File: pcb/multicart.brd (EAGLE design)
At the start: 55.5 x 85.1 mm, 13 parts, among them IC1 74HCT373N, IC2 M27C4001B, Q1 BS170

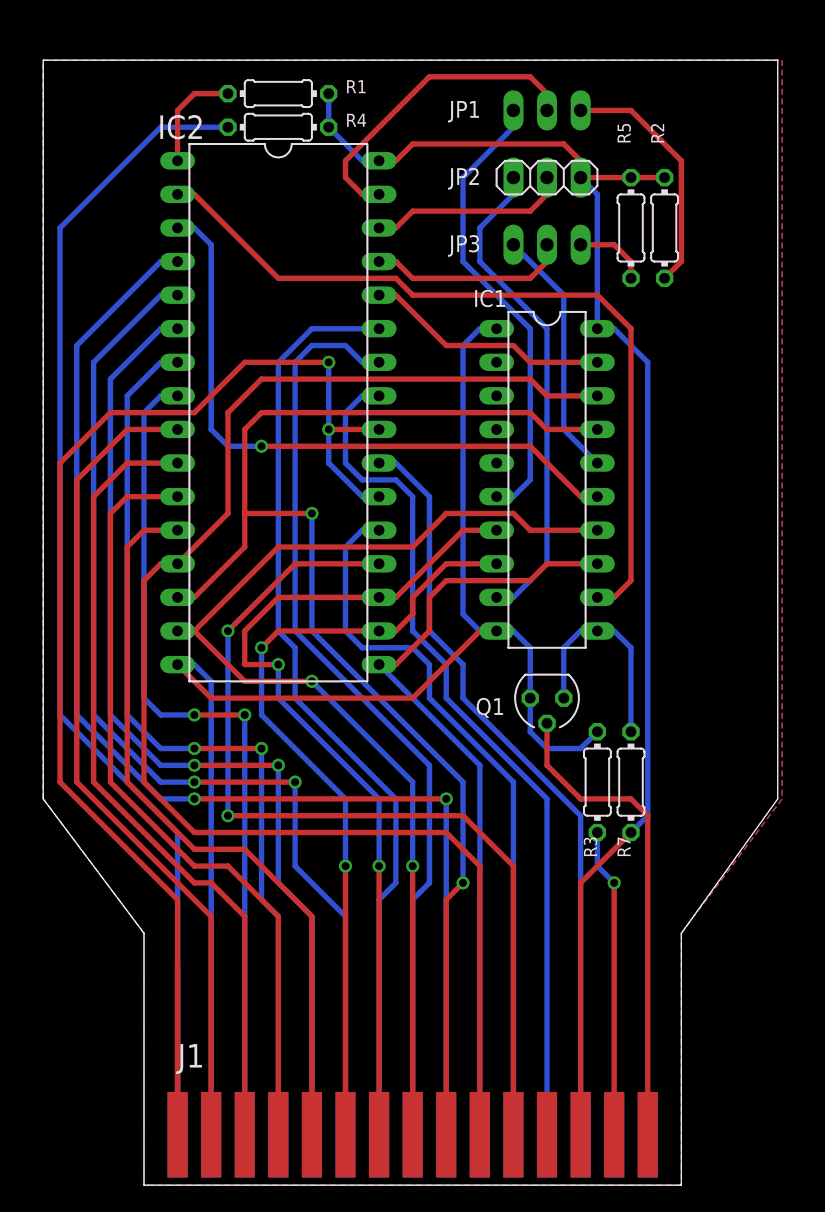
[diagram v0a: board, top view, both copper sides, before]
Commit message: Swapped cart bank mapping & reorganized the PCB.
Fixes #1
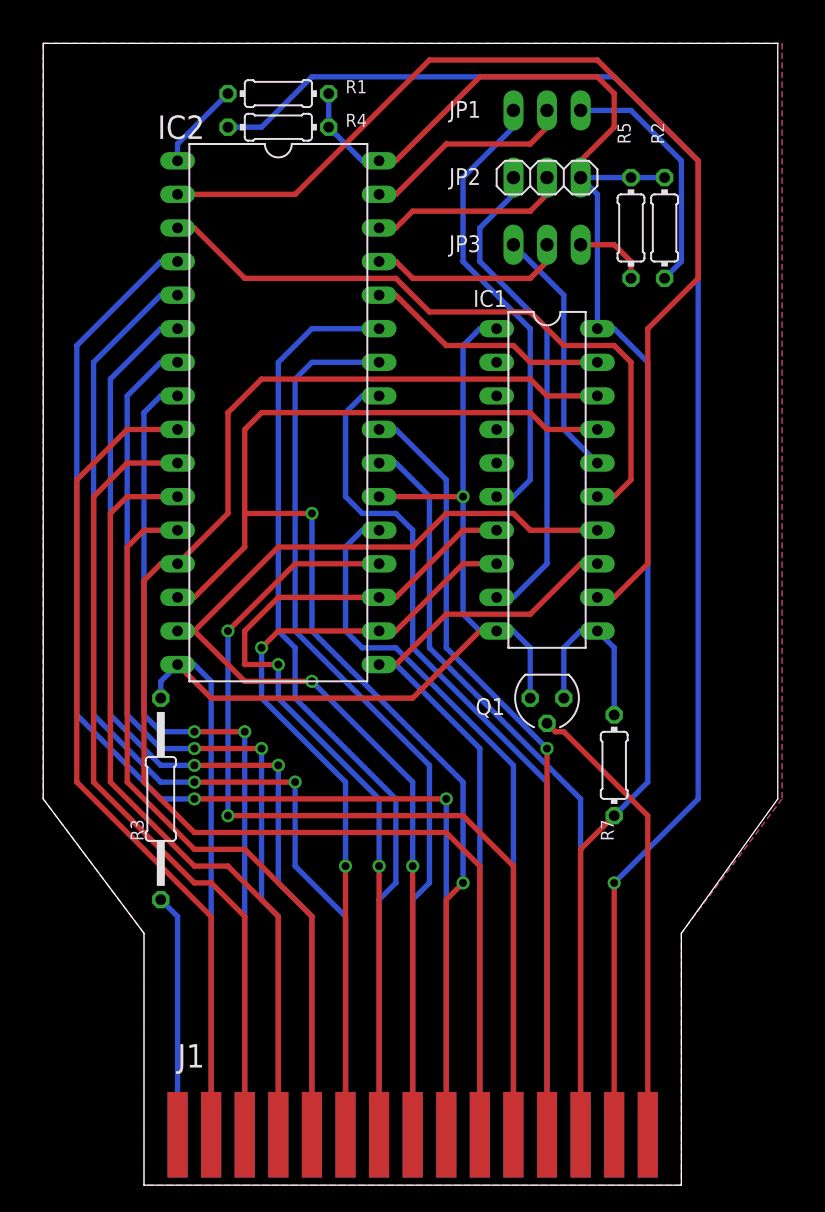
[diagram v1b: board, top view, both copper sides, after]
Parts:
- R3: device resistor:0204/7 -> resistor:0207/15
- moved R3 33.0 mm to (15.2, 26.7)
- moved R7 1.80 mm to (49.5, 29.2)
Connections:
- net GND: now also IC2.22
- net N$13: now also J1.14; no longer J1.A
- net N$14: now also J1.A; no longer J1.14
- net N$17: now also J1.12; no longer IC2.22, J1.1
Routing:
- net N$17: track 107.0 -> 59.3 mm, vias 2 -> 1
- net N$13: track 88.1 -> 116.1 mm, vias 0 -> 1
- net N$4: track 60.6 -> 83.7 mm
- net VCC: track 108.7 -> 119.4 mm
- net N$10: track 24.0 -> 16.1 mm
- net N$14: track 23.4 -> 18.3 mm, vias 1 -> 0
- net N$7: track 16.3 -> 13.8 mm
- net N$3: track 48.4 -> 50.5 mm, vias 1 -> 0
- net N$8: track 36.5 -> 34.6 mm
- net A9: track 70.6 -> 68.8 mm
- net N$9: track 8.15 -> 6.66 mm
- net GND: track 106.6 -> 107.4 mm, vias 0 -> 1
- net D3: track 59.9 -> 59.1 mm
- net D7: track 55.0 -> 54.3 mm
- net D4: track 60.6 -> 59.9 mm
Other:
- board size 55.5 x 85.1 mm -> 55.5 x 86.4 mm

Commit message: Optimized the design.
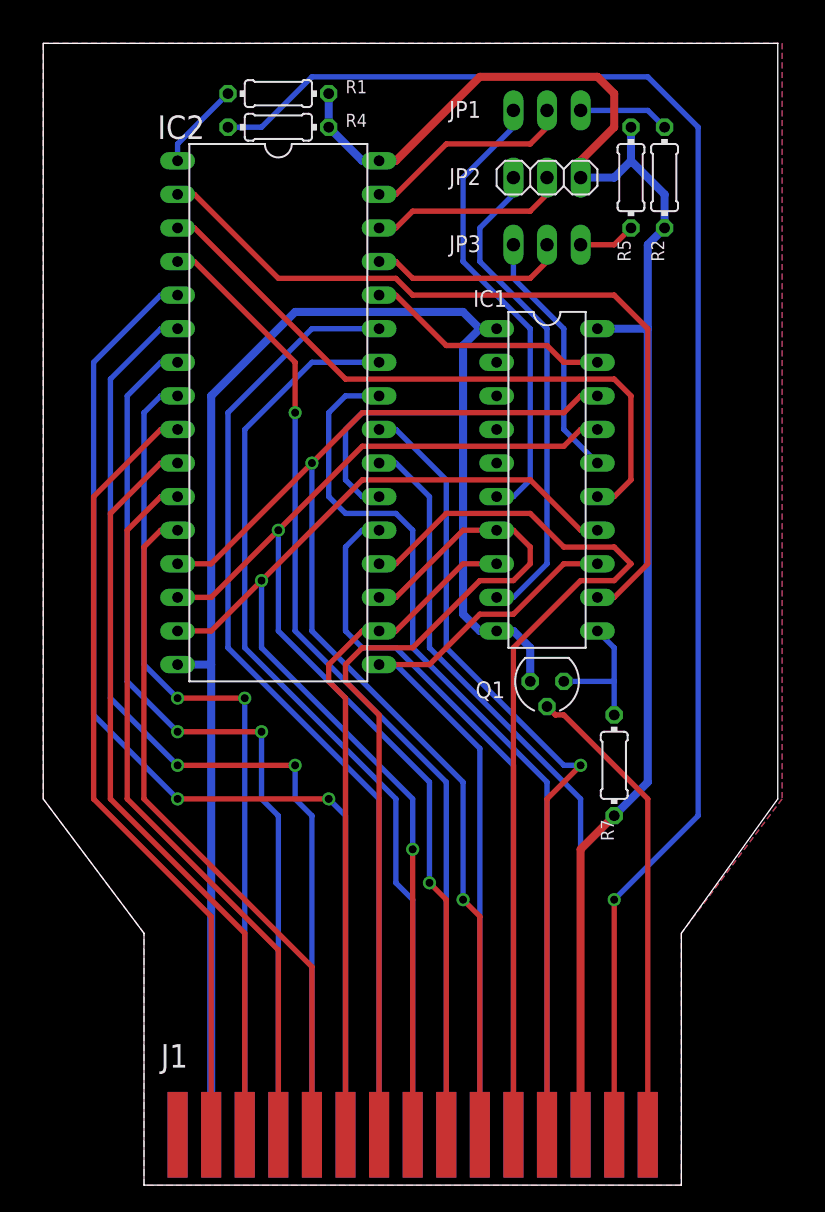
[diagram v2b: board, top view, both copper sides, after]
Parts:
- removed R3: 4k7, resistor:0207/15
- moved R2 3.81 mm to (53.3, 73.7), turned to 270 degrees
- moved R5 3.81 mm to (50.8, 73.7)
- moved Q1 1.27 mm to (44.5, 35.6)
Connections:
- removed net N$14: J1.A, R3.2
- net GND: no longer R3.1
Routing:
- net GND: track 107.4 -> 130.2 mm, vias 1 -> 0
- net N$4: track 83.7 -> 62.4 mm
- net A12: track 94.2 -> 75.2 mm, vias 2 -> 1
- net N$14: track 18.3 -> 0.00 mm
- net D0: track 109.2 -> 93.1 mm, vias 0 -> 2
- net D1: track 100.6 -> 88.0 mm
- net N$11: track 18.6 -> 6.88 mm
- net D4: track 59.9 -> 51.9 mm, vias 2 -> 0
- net VCC: track 119.4 -> 123.8 mm
- net A1: track 59.3 -> 55.3 mm
- net A0: track 56.8 -> 52.8 mm
- net A2: track 61.1 -> 57.9 mm
- net N$7: track 13.8 -> 10.7 mm
- net D5: track 66.0 -> 69.1 mm, vias 2 -> 0
- net N$17: track 59.3 -> 62.2 mm
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
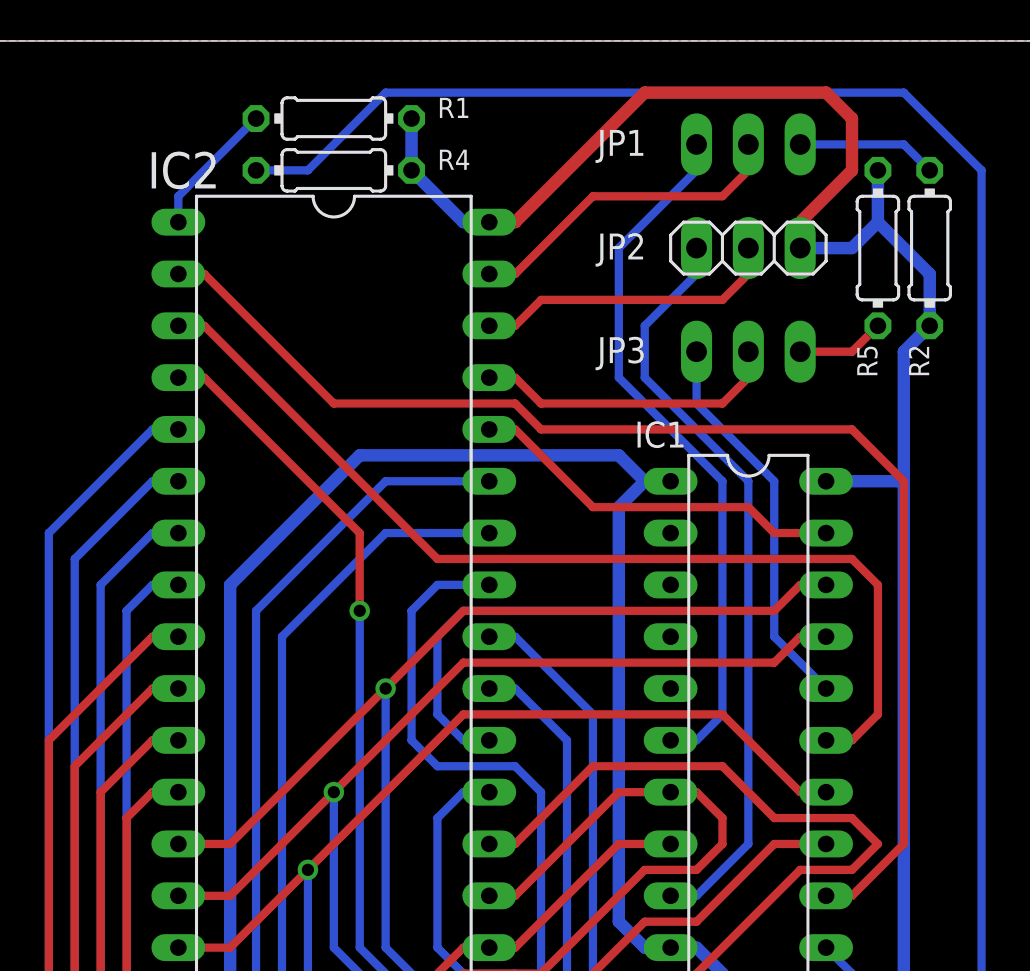
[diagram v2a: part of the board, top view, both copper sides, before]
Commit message: Added bypass caps to the design.
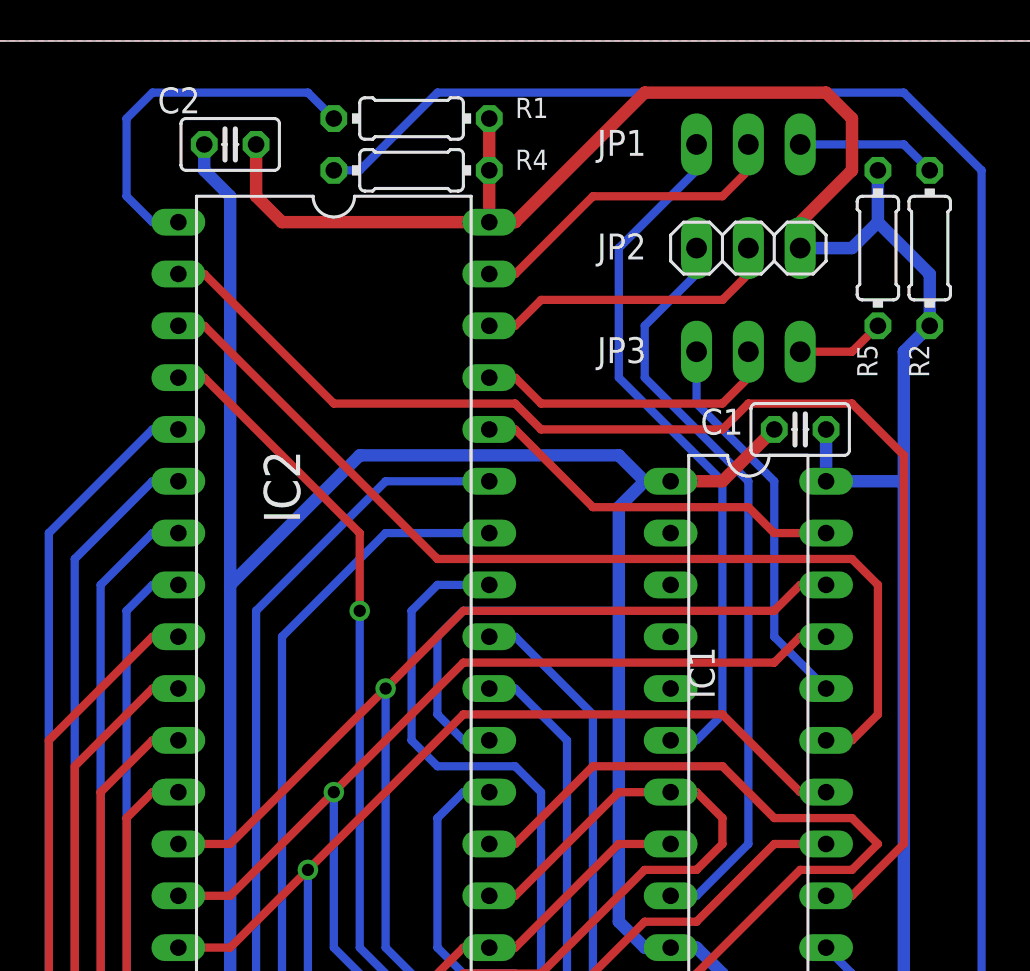
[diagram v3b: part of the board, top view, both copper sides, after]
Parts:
- added C1, C2: 100n, resistor:C025-025X050
- moved R1 3.81 mm to (27.9, 80.0)
- moved R4 3.81 mm to (27.9, 77.5)
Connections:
- net GND: now also C1.2, C2.2
- net VCC: now also C1.1, C2.1
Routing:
- net GND: track 130.2 -> 158.5 mm
- net VCC: track 123.8 -> 138.5 mm
- net N$9: track 6.66 -> 18.1 mm
- net N$13: track 117.5 -> 113.7 mm
- net N$4: track 62.4 -> 64.2 mm
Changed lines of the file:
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@@
 <layer number="45" name="Holes" color="7" fill="1" visible="yes" active="yes"/>
 <layer number="46" name="Milling" color="3" fill="1" visible="yes" active="yes"/>
-<layer number="47" name="Measures" color="7" fill="1" visible="yes" active="yes"/>
+<layer number="47" name="Measures" color="7" fill="1" visible="no" active="yes"/>
 <layer number="48" name="Document" color="7" fill="1" visible="yes" active="yes"/>
 <layer number="49" name="Reference" color="7" fill="1" visible="yes" active="yes"/>
@@
 <elements>
 <element name="IC1" library="74xx-eu" package="DIL20" value="74HCT373N" x="44.45" y="50.8" smashed="yes" rot="R270">
-<attribute name="NAME" x="38.862" y="63.881" size="1.27" layer="25"/>
+<attribute name="NAME" x="42.799" y="51.562" size="1.27" layer="25" rot="R90"/>
 <attribute name="VALUE" x="44.069" y="60.579" size="1.27" layer="27" rot="R270"/>
 </element>
@@
 <attribute name="MPN" value="M27C4001-10B1" x="24.13" y="55.88" size="1.778" layer="27" rot="R270" display="off"/>
 <attribute name="MF" value="" x="24.13" y="55.88" size="1.778" layer="27" rot="R270" display="off"/>
-<attribute name="NAME" x="14.986" y="76.581" size="1.778" layer="25"/>
+<attribute name="NAME" x="20.701" y="63.754" size="1.778" layer="25" rot="R270"/>
 <attribute name="VALUE" x="23.241" y="72.771" size="1.778" layer="27" rot="R270"/>
 </element>
@@
 </element>
 <element name="Q1" library="transistor-small-signal" package="SOT54E" value="BS170" x="44.45" y="35.56" rot="R180"/>
-<element name="R1" library="resistor" package="0204/7" value="4k7" x="24.13" y="80.01" smashed="yes">
-<attribute name="NAME" x="29.21" y="80.0354" size="0.9906" layer="25" ratio="10"/>
-<attribute name="VALUE" x="23.7744" y="79.5274" size="0.9906" layer="27" ratio="10"/>
+<element name="R1" library="resistor" package="0204/7" value="4k7" x="27.94" y="80.01" smashed="yes">
+<attribute name="NAME" x="33.02" y="80.0354" size="0.9906" layer="25" ratio="10"/>
+<attribute name="VALUE" x="27.5844" y="79.5274" size="0.9906" layer="27" ratio="10"/>
 </element>
 <element name="R2" library="resistor" package="0204/7" value="4k7" x="53.34" y="73.66" smashed="yes" rot="R270">
@@
 <attribute name="VALUE" x="53.1876" y="73.3044" size="0.9906" layer="27" ratio="10" rot="R90"/>
 </element>
-<element name="R4" library="resistor" package="0204/7" value="4k7" x="24.13" y="77.47" smashed="yes" rot="R180">
-<attribute name="NAME" x="29.21" y="77.4954" size="0.9906" layer="25" ratio="10"/>
-<attribute name="VALUE" x="23.7744" y="76.9874" size="0.9906" layer="27" ratio="10"/>
+<element name="R4" library="resistor" package="0204/7" value="4k7" x="27.94" y="77.47" smashed="yes" rot="R180">
+<attribute name="NAME" x="33.02" y="77.4954" size="0.9906" layer="25" ratio="10"/>
+<attribute name="VALUE" x="27.5844" y="76.9874" size="0.9906" layer="27" ratio="10"/>
 </element>
 <element name="R5" library="resistor" package="0204/7" value="4k7" x="50.8" y="73.66" smashed="yes" rot="R90">
@@
 <attribute name="NAME" x="49.5046" y="23.495" size="0.9906" layer="25" ratio="10" rot="R90"/>
 <attribute name="VALUE" x="49.3776" y="28.8544" size="0.9906" layer="27" ratio="10" rot="R90"/>
+</element>
+<element name="C1" library="resistor" package="C025-025X050" value="100n" x="46.99" y="64.77" smashed="yes" rot="R180">
+<attribute name="NAME" x="44.196" y="65.786" size="1.27" layer="25" ratio="10" rot="R180"/>
+<attribute name="VALUE" x="49.784" y="64.516" size="1.27" layer="27" ratio="10"/>
+</element>
+<element name="C2" library="resistor" package="C025-025X050" value="100n" x="19.05" y="78.74" smashed="yes" rot="R180">
+<attribute name="NAME" x="15.494" y="80.264" size="1.27" layer="25" ratio="10"/>
+<attribute name="VALUE" x="22.606" y="81.534" size="1.27" layer="27" ratio="10" rot="R180"/>
 </element>
 </elements>
@@
 <wire x1="48.26" y1="41.91" x2="49.53" y2="41.91" width="0.4064" layer="1"/>
 <wire x1="49.53" y1="41.91" x2="52.07" y2="44.45" width="0.4064" layer="1"/>
-<wire x1="52.07" y1="44.45" x2="52.07" y2="62.23" width="0.4064" layer="1"/>
-<wire x1="52.07" y1="62.23" x2="49.53" y2="64.77" width="0.4064" layer="1"/>
-<wire x1="49.53" y1="64.77" x2="34.29" y2="64.77" width="0.4064" layer="1"/>
+<wire x1="52.07" y1="44.45" x2="52.07" y2="63.5" width="0.4064" layer="1"/>
 <wire x1="34.29" y1="64.77" x2="33.02" y2="66.04" width="0.4064" layer="1"/>
 <wire x1="33.02" y1="66.04" x2="24.13" y2="66.04" width="0.4064" layer="1"/>
 <wire x1="24.13" y1="66.04" x2="17.78" y2="72.39" width="0.4064" layer="1"/>
 <wire x1="17.78" y1="72.39" x2="16.51" y2="72.39" width="0.4064" layer="1"/>
+<wire x1="44.45" y1="66.04" x2="43.18" y2="64.77" width="0.4064" layer="1"/>
+<wire x1="43.18" y1="64.77" x2="34.29" y2="64.77" width="0.4064" layer="1"/>
+<wire x1="44.45" y1="66.04" x2="49.53" y2="66.04" width="0.4064" layer="1"/>
+<wire x1="49.53" y1="66.04" x2="52.07" y2="63.5" width="0.4064" layer="1"/>
 </signal>
 <signal name="D0">
@@
 <contactref element="R2" pad="2"/>
 <contactref element="R5" pad="2"/>
-<wire x1="27.94" y1="80.01" x2="27.94" y2="77.47" width="0.6096" layer="16"/>
-<wire x1="27.94" y1="77.47" x2="30.48" y2="74.93" width="0.6096" layer="16"/>
-<wire x1="30.48" y1="74.93" x2="31.75" y2="74.93" width="0.6096" layer="16"/>
 <wire x1="49.53" y1="25.4" x2="52.07" y2="27.94" width="0.6096" layer="16"/>
 <wire x1="52.07" y1="27.94" x2="52.07" y2="62.23" width="0.6096" layer="16"/>
@@
 <wire x1="50.8" y1="77.47" x2="50.8" y2="74.93" width="0.6096" layer="16"/>
 <wire x1="50.8" y1="74.93" x2="53.34" y2="72.39" width="0.6096" layer="16"/>
+<wire x1="46.99" y1="73.66" x2="49.53" y2="73.66" width="0.6096" layer="16"/>
+<wire x1="49.53" y1="73.66" x2="50.8" y2="74.93" width="0.6096" layer="16"/>
+<contactref element="C1" pad="1"/>
+<contactref element="C2" pad="1"/>
+<wire x1="31.75" y1="74.93" x2="31.75" y2="77.47" width="0.6096" layer="1"/>
+<wire x1="31.75" y1="77.47" x2="31.75" y2="80.01" width="0.6096" layer="1"/>
+<wire x1="20.32" y1="78.74" x2="20.32" y2="76.2" width="0.6096" layer="1"/>
+<wire x1="20.32" y1="76.2" x2="21.59" y2="74.93" width="0.6096" layer="1"/>
+<wire x1="21.59" y1="74.93" x2="31.75" y2="74.93" width="0.6096" layer="1"/>
+<wire x1="48.26" y1="64.77" x2="48.26" y2="62.23" width="0.6096" layer="16"/>
 <wire x1="52.07" y1="62.23" x2="52.07" y2="68.58" width="0.6096" layer="16"/>
 <wire x1="52.07" y1="68.58" x2="53.34" y2="69.85" width="0.6096" layer="16"/>
-<wire x1="46.99" y1="73.66" x2="49.53" y2="73.66" width="0.6096" layer="16"/>
-<wire x1="49.53" y1="73.66" x2="50.8" y2="74.93" width="0.6096" layer="16"/>
 </signal>
 <signal name="GND">
@@
 <wire x1="41.91" y1="39.37" x2="43.18" y2="38.1" width="0.6096" layer="16"/>
 <wire x1="43.18" y1="38.1" x2="43.18" y2="35.56" width="0.6096" layer="16"/>
+<contactref element="C1" pad="2"/>
+<contactref element="C2" pad="2"/>
+<wire x1="17.78" y1="78.74" x2="17.78" y2="77.47" width="0.6096" layer="16"/>
+<wire x1="17.78" y1="77.47" x2="19.05" y2="76.2" width="0.6096" layer="16"/>
+<wire x1="19.05" y1="76.2" x2="19.05" y2="57.15" width="0.6096" layer="16"/>
+<wire x1="40.64" y1="62.23" x2="43.18" y2="62.23" width="0.6096" layer="1"/>
+<wire x1="43.18" y1="62.23" x2="45.72" y2="64.77" width="0.6096" layer="1"/>
 </signal>
 <signal name="N$9">
 <contactref element="IC2" pad="1"/>
 <contactref element="R1" pad="1"/>
-<wire x1="16.51" y1="74.93" x2="16.51" y2="76.2" width="0.4064" layer="16"/>
-<wire x1="16.51" y1="76.2" x2="20.32" y2="80.01" width="0.4064" layer="16"/>
+<wire x1="16.51" y1="74.93" x2="15.24" y2="74.93" width="0.4064" layer="16"/>
+<wire x1="15.24" y1="74.93" x2="13.97" y2="76.2" width="0.4064" layer="16"/>
+<wire x1="13.97" y1="76.2" x2="13.97" y2="80.01" width="0.4064" layer="16"/>
+<wire x1="13.97" y1="80.01" x2="15.24" y2="81.28" width="0.4064" layer="16"/>
+<wire x1="15.24" y1="81.28" x2="22.86" y2="81.28" width="0.4064" layer="16"/>
+<wire x1="22.86" y1="81.28" x2="24.13" y2="80.01" width="0.4064" layer="16"/>
 </signal>
 <signal name="N$5">
@@
 <contactref element="J1" pad="14"/>
 <contactref element="R4" pad="2"/>
-<wire x1="20.32" y1="77.47" x2="22.86" y2="77.47" width="0.4064" layer="16"/>
-<wire x1="22.86" y1="77.47" x2="26.67" y2="81.28" width="0.4064" layer="16"/>
-<wire x1="26.67" y1="81.28" x2="52.07" y2="81.28" width="0.4064" layer="16"/>
+<wire x1="24.13" y1="77.47" x2="25.4" y2="77.47" width="0.4064" layer="16"/>
+<wire x1="25.4" y1="77.47" x2="29.21" y2="81.28" width="0.4064" layer="16"/>
+<wire x1="29.21" y1="81.28" x2="52.07" y2="81.28" width="0.4064" layer="16"/>
 <wire x1="55.88" y1="77.47" x2="55.88" y2="25.4" width="0.4064" layer="16"/>
 <wire x1="55.88" y1="25.4" x2="49.53" y2="19.05" width="0.4064" layer="16"/>
